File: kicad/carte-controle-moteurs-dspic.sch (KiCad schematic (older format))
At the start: 72 parts, among them J1 PDB, J10 PWR_IN, J11 GND, J12 5V, J13 3.3V, J14 EN, J15 MOTEUR 1, J16 MOTEUR 2, J17 L1, J18 H1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

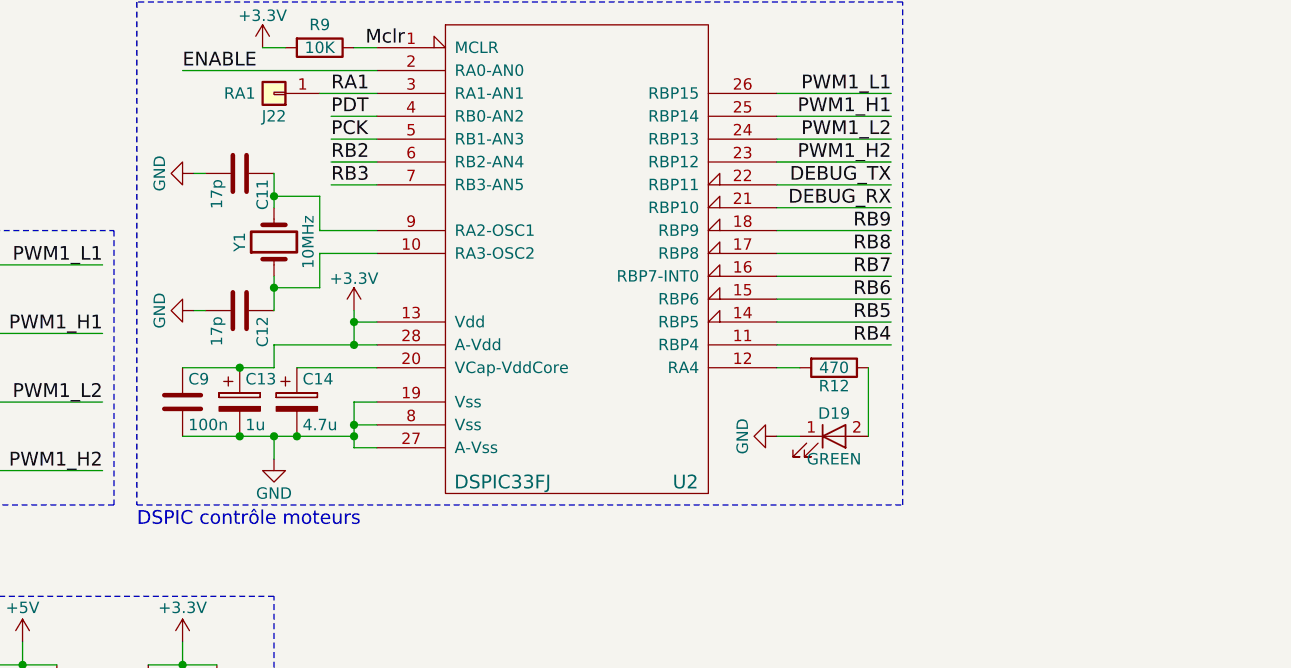
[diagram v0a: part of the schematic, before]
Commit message: Ajout d'un lot de capacités pour la patte 28 du DsPIC
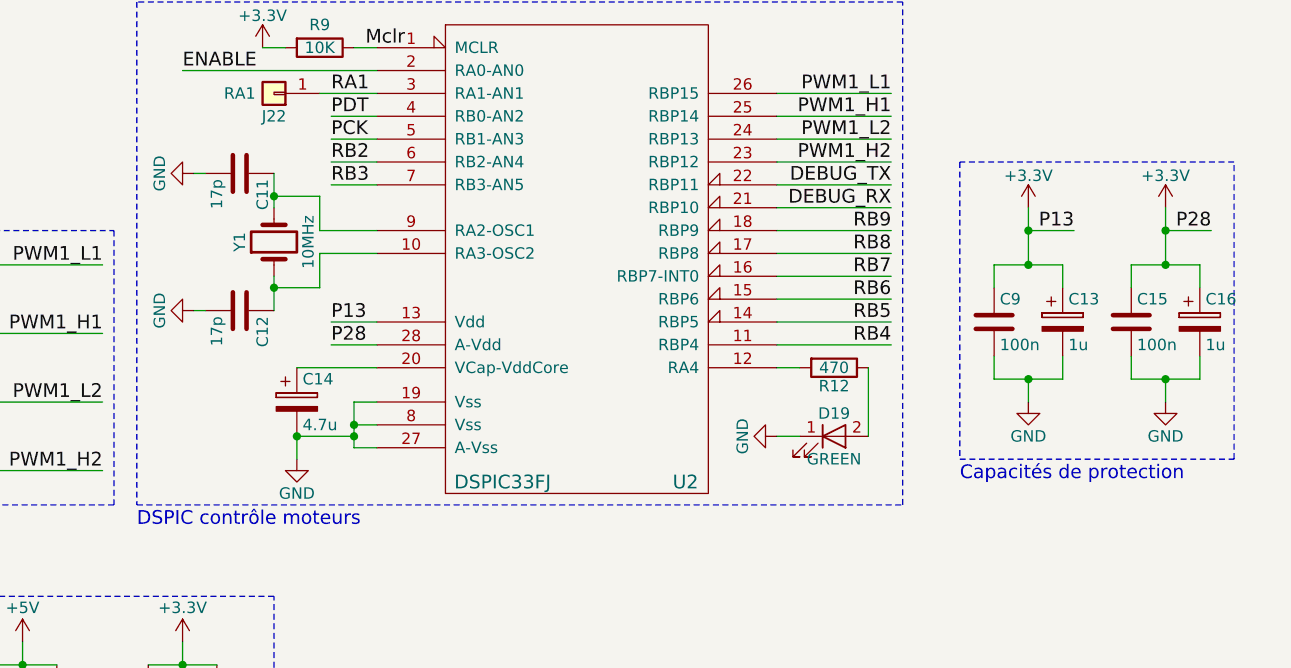
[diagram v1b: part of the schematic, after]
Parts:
- added C15: 100n, Capacitors_THT:C_Rect_L7.0mm_W3.5mm_P2.50mm_P5.00mm, symbol C
- added C16: 1u, Capacitors_THT:CP_Radial_D10.0mm_P2.50mm_P5.00mm, symbol CP
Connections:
- net +3V3: now also C15.1, C16.1
- net GND: now also C15.2, C16.2
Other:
- note added: "Capacités de protection"
- moved on the sheet: C13, C9
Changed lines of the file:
@@
 Wire Notes Line
 	8600 2350 6850 2350
-Connection ~ 6250 4850
-Wire Wire Line
-	6250 4800 6250 4950
 Connection ~ 6250 5350
 Wire Wire Line
@@
 Connection ~ 6000 5350
 Wire Wire Line
-	5500 5350 6250 5350
+	6000 5350 6250 5350
 Connection ~ 3450 2650
 Wire Wire Line
@@
 	2900 2050 4550 2050
 Wire Wire Line
-	5900 4950 6350 4950
-Connection ~ 5750 5350
-Wire Wire Line
 	1050 6700 1650 6700
 Wire Wire Line
@@
 Wire Wire Line
 	8600 4350 8100 4350
-Wire Wire Line
-	6250 4850 6350 4850
-Connection ~ 6250 4950
 Wire Wire Line
 	1050 3900 1550 3900
@@
 L C C9
 U 1 1 5A837AE4
-P 5500 5200
-F 0 "C9" H 5525 5300 50  0000 L CNN
-F 1 "100n" H 5525 5100 50  0000 L CNN
-F 2 "Capacitors_THT:C_Rect_L7.0mm_W3.5mm_P2.50mm_P5.00mm" H 5538 5050 50  0001 C CNN
-F 3 "" H 5500 5200 50  0001 C CNN
-	1    5500 5200
+P 9050 4850
+F 0 "C9" H 9075 4950 50  0000 L CNN
+F 1 "100n" H 9075 4750 50  0000 L CNN
+F 2 "Capacitors_THT:C_Rect_L7.0mm_W3.5mm_P2.50mm_P5.00mm" H 9088 4700 50  0001 C CNN
+F 3 "" H 9050 4850 50  0001 C CNN
+	1    9050 4850
 	1    0    0    -1
 $EndComp
@@
 L CP C13
 U 1 1 5A837CD2
-P 5750 5200
-F 0 "C13" H 5775 5300 50  0000 L CNN
-F 1 "1u" H 5775 5100 50  0000 L CNN
-F 2 "Capacitors_THT:CP_Radial_D10.0mm_P2.50mm_P5.00mm" H 5788 5050 50  0001 C CNN
-F 3 "" H 5750 5200 50  0001 C CNN
-	1    5750 5200
+P 9350 4850
+F 0 "C13" H 9375 4950 50  0000 L CNN
+F 1 "1u" H 9375 4750 50  0000 L CNN
+F 2 "Capacitors_THT:CP_Radial_D10.0mm_P2.50mm_P5.00mm" H 9388 4700 50  0001 C CNN
+F 3 "" H 9350 4850 50  0001 C CNN
+	1    9350 4850
 	1    0    0    -1
 $EndComp
@@
 L GND #PWR028
 U 1 1 5A8385EE
-P 5900 5450
-F 0 "#PWR028" H 5900 5200 50  0001 C CNN
-F 1 "GND" H 5900 5300 50  0000 C CNN
-F 2 "" H 5900 5450 50  0001 C CNN
-F 3 "" H 5900 5450 50  0001 C CNN
-	1    5900 5450
-	1    0    0    -1
-$EndComp
-Wire Wire Line
-	5900 5350 5900 5450
-Connection ~ 5900 5350
+P 6000 5450
+F 0 "#PWR028" H 6000 5200 50  0001 C CNN
+F 1 "GND" H 6000 5300 50  0000 C CNN
+F 2 "" H 6000 5450 50  0001 C CNN
+F 3 "" H 6000 5450 50  0001 C CNN
+	1    6000 5450
+	1    0    0    -1
+$EndComp
 $Comp
 L C C11
@@
 	0    -1   -1   0
 $EndComp
-Wire Wire Line
-	5500 5050 5900 5050
-Wire Wire Line
-	5900 5050 5900 4950
-Connection ~ 5750 5050
 $Comp
 L +3.3V #PWR031
 U 1 1 5A83ABE5
-P 6250 4800
-F 0 "#PWR031" H 6250 4650 50  0001 C CNN
-F 1 "+3.3V" H 6250 4940 50  0000 C CNN
-F 2 "" H 6250 4800 50  0001 C CNN
-F 3 "" H 6250 4800 50  0001 C CNN
-	1    6250 4800
+P 9200 4350
+F 0 "#PWR031" H 9200 4200 50  0001 C CNN
+F 1 "+3.3V" H 9200 4490 50  0000 C CNN
+F 2 "" H 9200 4350 50  0001 C CNN
+F 3 "" H 9200 4350 50  0001 C CNN
+	1    9200 4350
 	1    0    0    -1
 $EndComp
@@
 Text Notes 4400 7050 0    60   ~ 0
 Lissage tensions
+Wire Wire Line
+	6000 5350 6000 5450
+Wire Wire Line
+	6350 4850 6150 4850
+Wire Wire Line
+	6350 4950 6150 4950
+Text Label 6150 4850 0    60   ~ 0
+P13
+Text Label 6150 4950 0    60   ~ 0
+P28
+$Comp
+L GND #PWR042
+U 1 1 5A899D83
+P 9200 5200
+F 0 "#PWR042" H 9200 4950 50  0001 C CNN
+F 1 "GND" H 9200 5050 50  0000 C CNN
+F 2 "" H 9200 5200 50  0001 C CNN
+F 3 "" H 9200 5200 50  0001 C CNN
+	1    9200 5200
+	1    0    0    -1
+$EndComp
+Wire Wire Line
+	9050 5000 9050 5100
+Wire Wire Line
+	9050 5100 9350 5100
+Wire Wire Line
+	9350 5100 9350 5000
+Wire Wire Line
+	9200 5100 9200 5200
+Connection ~ 9200 5100
+Wire Wire Line
+	9050 4700 9050 4600
+Wire Wire Line
+	9050 4600 9350 4600
+Wire Wire Line
+	9350 4600 9350 4700
+Wire Wire Line
+	9200 4350 9200 4600
+Connection ~ 9200 4600
+Wire Wire Line
+	9200 4450 9400 4450
+Connection ~ 9200 4450
+Text Label 9400 4450 2    60   ~ 0
+P13
+$Comp
+L C C15
+U 1 1 5A89A9B0
+P 9650 4850
+F 0 "C15" H 9675 4950 50  0000 L CNN
+F 1 "100n" H 9675 4750 50  0000 L CNN
+F 2 "Capacitors_THT:C_Rect_L7.0mm_W3.5mm_P2.50mm_P5.00mm" H 9688 4700 50  0001 C CNN
+F 3 "" H 9650 4850 50  0001 C CNN
+	1    9650 4850
+	1    0    0    -1
+$EndComp
+$Comp
+L CP C16
+U 1 1 5A89A9B6
+P 9950 4850
+F 0 "C16" H 9975 4950 50  0000 L CNN
+F 1 "1u" H 9975 4750 50  0000 L CNN
+F 2 "Capacitors_THT:CP_Radial_D10.0mm_P2.50mm_P5.00mm" H 9988 4700 50  0001 C CNN
+F 3 "" H 9950 4850 50  0001 C CNN
+	1    9950 4850
+	1    0    0    -1
+$EndComp
+$Comp
+L +3.3V #PWR043
+U 1 1 5A89A9BC
+P 9800 4350
+F 0 "#PWR043" H 9800 4200 50  0001 C CNN
+F 1 "+3.3V" H 9800 4490 50  0000 C CNN
+F 2 "" H 9800 4350 50  0001 C CNN
+F 3 "" H 9800 4350 50  0001 C CNN
+	1    9800 4350
+	1    0    0    -1
+$EndComp
+$Comp
+L GND #PWR044
+U 1 1 5A89A9C2
+P 9800 5200
+F 0 "#PWR044" H 9800 4950 50  0001 C CNN
+F 1 "GND" H 9800 5050 50  0000 C CNN
+F 2 "" H 9800 5200 50  0001 C CNN
+F 3 "" H 9800 5200 50  0001 C CNN
+	1    9800 5200
+	1    0    0    -1
+$EndComp
+Wire Wire Line
+	9650 5000 9650 5100
+Wire Wire Line
+	9650 5100 9950 5100
+Wire Wire Line
+	9950 5100 9950 5000
+Wire Wire Line
+	9800 5100 9800 5200
+Connection ~ 9800 5100
+Wire Wire Line
+	9650 4700 9650 4600
+Wire Wire Line
+	9650 4600 9950 4600
+Wire Wire Line
+	9950 4600 9950 4700
+Wire Wire Line
+	9800 4350 9800 4600
+Connection ~ 9800 4600
+Wire Wire Line
+	9800 4450 10000 4450
+Connection ~ 9800 4450
+Text Label 10000 4450 2    60   ~ 0
+P28
+Wire Notes Line
+	8900 4150 8900 5450
+Wire Notes Line
+	8900 5450 10100 5450
+Wire Notes Line
+	10100 5450 10100 4150
+Wire Notes Line
+	10100 4150 8900 4150
+Text Notes 8900 5550 0    60   ~ 0
+Capacités de protection
 $EndSCHEMATC
